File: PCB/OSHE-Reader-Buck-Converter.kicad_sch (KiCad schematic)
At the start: 18 parts, among them U1 TPS5432DDA

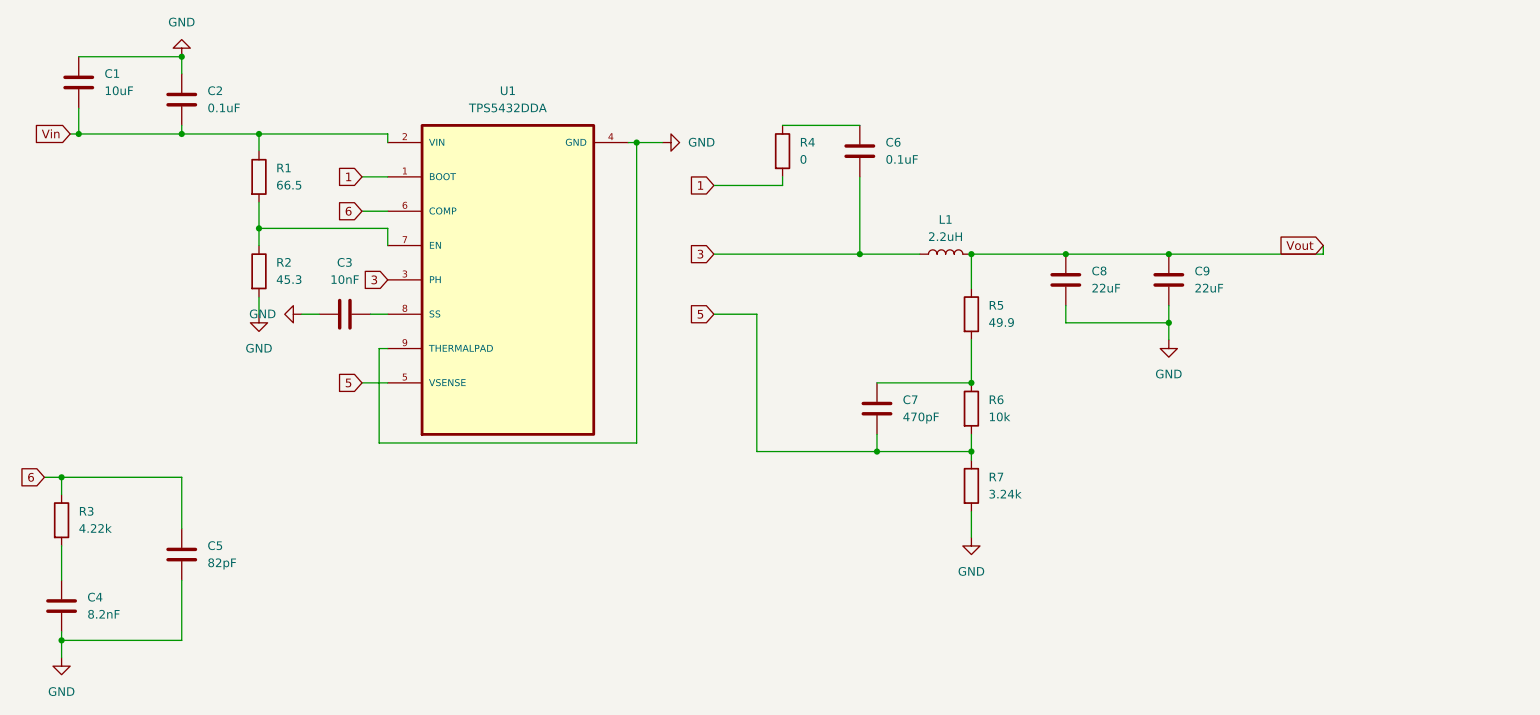
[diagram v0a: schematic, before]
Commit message: added hierarchical symbols to Buck, and did miscelaneous fixes
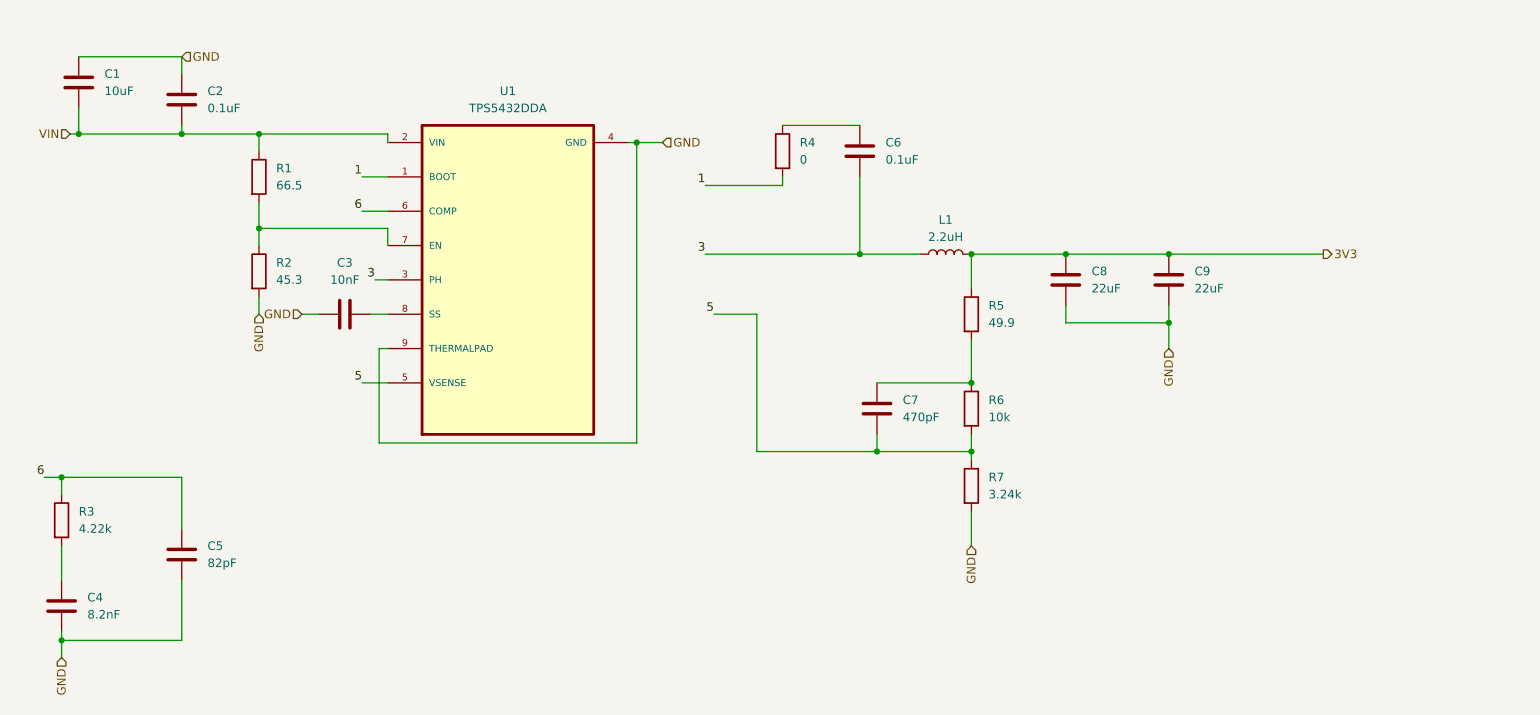
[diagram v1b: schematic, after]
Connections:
- net Vin  renamed VIN
- net Vout renamed 3V3

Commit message: fixed up the pcb so everything is *basically* passing ERC
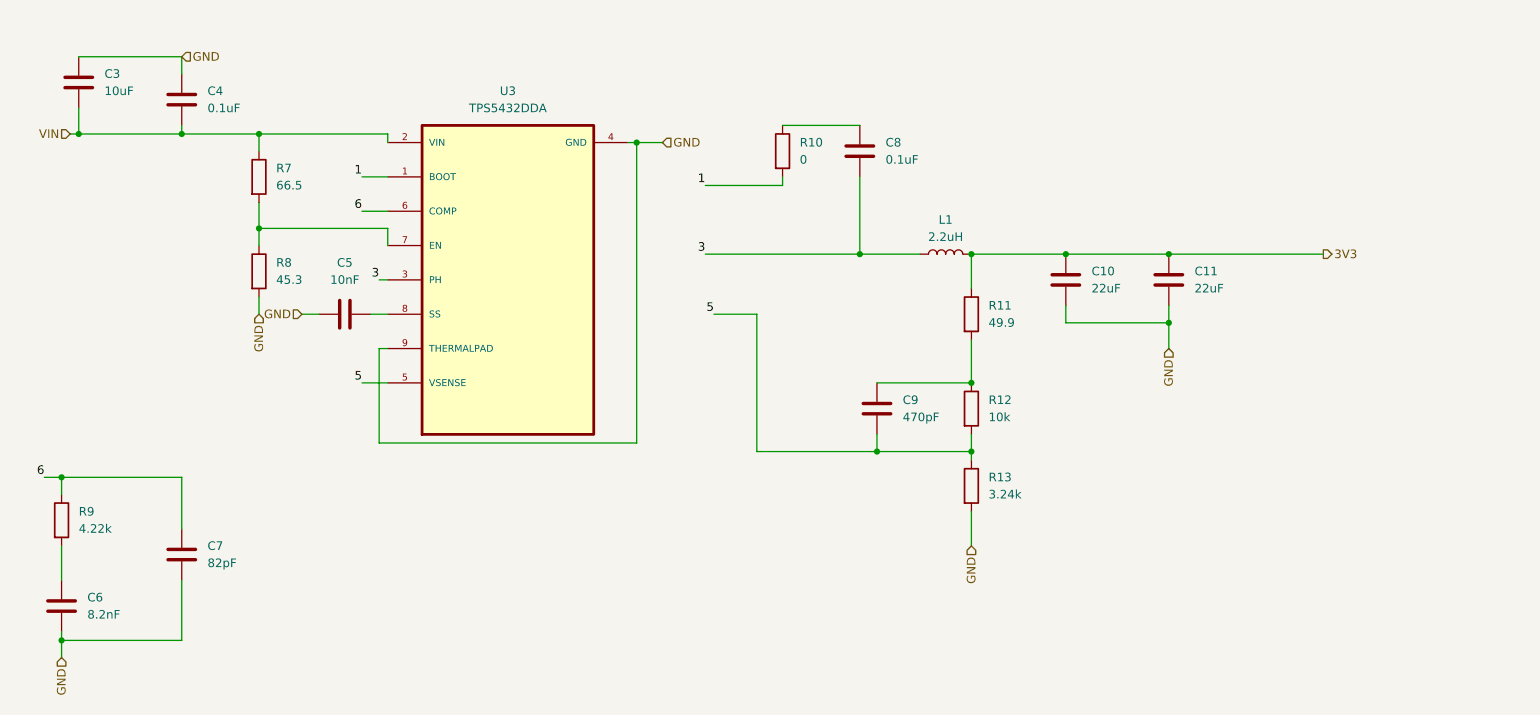
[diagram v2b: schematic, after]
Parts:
- U3: renamed from U1; footprint TPS5432DDA:VREG_LM5017MR_NOPB -> TPS5432DDAR:DDA_R-PDSO-G8_TEX
- renumbered C8 to C10, C9 to C11, C1 to C3, C2 to C4, C3 to C5, C4 to C6, C5 to C7, C6 to C8, C7 to C9, R4 to R10, R5 to R11, R6 to R12, R7 to R13, R1 to R7, R2 to R8, R3 to R9
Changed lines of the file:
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@@
 	(wire
 		(pts
-			(xy 75.565 48.26) (xy 77.47 48.26)
+			(xy 76.2 48.26) (xy 77.47 48.26)
 		)
 		(stroke
@@
 	)
 	(label "3"
-		(at 75.565 48.26 180)
+		(at 76.2 48.26 180)
 		(effects
 			(font
@@
 		(dnp no)
 		(fields_autoplaced yes)
-		(property "Reference" "R3"
+		(property "Reference" "R9"
 			(at 31.75 82.5499 0)
 			(effects
@@
 			(project "OSHE-Reader-PCB"
 				(path "/3f072c92-e35a-4654-839b-728bd3dc3a46/ae251da9-64d7-46e8-9279-c40d7a440224"
-					(reference "R3")
+					(reference "R9")
 					(unit 1)
 				)
@@
 		(dnp no)
 		(fields_autoplaced yes)
-		(property "Reference" "C9"
+		(property "Reference" "C11"
 			(at 196.85 46.9899 0)
 			(effects
@@
 			(project "OSHE-Reader-PCB"
 				(path "/3f072c92-e35a-4654-839b-728bd3dc3a46/ae251da9-64d7-46e8-9279-c40d7a440224"
-					(reference "C9")
+					(reference "C11")
 					(unit 1)
 				)
@@
 		(dnp no)
 		(fields_autoplaced yes)
-		(property "Reference" "C8"
+		(property "Reference" "C10"
 			(at 181.61 46.9899 0)
 			(effects
@@
 			(project "OSHE-Reader-PCB"
 				(path "/3f072c92-e35a-4654-839b-728bd3dc3a46/ae251da9-64d7-46e8-9279-c40d7a440224"
-					(reference "C8")
+					(reference "C10")
 					(unit 1)
 				)
@@
 		(dnp no)
 		(fields_autoplaced yes)
-		(property "Reference" "R4"
+		(property "Reference" "R10"
 			(at 138.43 27.9399 0)
 			(effects
@@
 			(project "OSHE-Reader-PCB"
 				(path "/3f072c92-e35a-4654-839b-728bd3dc3a46/ae251da9-64d7-46e8-9279-c40d7a440224"
-					(reference "R4")
+					(reference "R10")
 					(unit 1)
 				)
@@
 		(dnp no)
 		(fields_autoplaced yes)
-		(property "Reference" "C5"
+		(property "Reference" "C7"
 			(at 50.8 87.6299 0)
 			(effects
@@
 			(project "OSHE-Reader-PCB"
 				(path "/3f072c92-e35a-4654-839b-728bd3dc3a46/ae251da9-64d7-46e8-9279-c40d7a440224"
-					(reference "C5")
+					(reference "C7")
 					(unit 1)
 				)
@@
 		(dnp no)
 		(fields_autoplaced yes)
-		(property "Reference" "R7"
+		(property "Reference" "R13"
 			(at 166.37 77.4699 0)
 			(effects
@@
 			(project "OSHE-Reader-PCB"
 				(path "/3f072c92-e35a-4654-839b-728bd3dc3a46/ae251da9-64d7-46e8-9279-c40d7a440224"
-					(reference "R7")
+					(reference "R13")
 					(unit 1)
 				)
@@
 		(dnp no)
 		(fields_autoplaced yes)
-		(property "Reference" "R1"
+		(property "Reference" "R7"
 			(at 60.96 31.7499 0)
 			(effects
@@
 			(project "OSHE-Reader-PCB"
 				(path "/3f072c92-e35a-4654-839b-728bd3dc3a46/ae251da9-64d7-46e8-9279-c40d7a440224"
-					(reference "R1")
+					(reference "R7")
 					(unit 1)
 				)
@@
 		(dnp no)
 		(fields_autoplaced yes)
-		(property "Reference" "R2"
+		(property "Reference" "R8"
 			(at 60.96 45.7199 0)
 			(effects
@@
 			(project "OSHE-Reader-PCB"
 				(path "/3f072c92-e35a-4654-839b-728bd3dc3a46/ae251da9-64d7-46e8-9279-c40d7a440224"
-					(reference "R2")
+					(reference "R8")
 					(unit 1)
 				)
@@
 		(dnp no)
 		(fields_autoplaced yes)
-		(property "Reference" "C4"
+		(property "Reference" "C6"
 			(at 33.02 95.2499 0)
 			(effects
@@
 			(project "OSHE-Reader-PCB"
 				(path "/3f072c92-e35a-4654-839b-728bd3dc3a46/ae251da9-64d7-46e8-9279-c40d7a440224"
-					(reference "C4")
+					(reference "C6")
 					(unit 1)
 				)
@@
 		(dnp no)
 		(fields_autoplaced yes)
-		(property "Reference" "R6"
+		(property "Reference" "R12"
 			(at 166.37 66.0399 0)
 			(effects
@@
 			(project "OSHE-Reader-PCB"
 				(path "/3f072c92-e35a-4654-839b-728bd3dc3a46/ae251da9-64d7-46e8-9279-c40d7a440224"
-					(reference "R6")
+					(reference "R12")
 					(unit 1)
 				)
@@
 		(dnp no)
 		(fields_autoplaced yes)
-		(property "Reference" "R5"
+		(property "Reference" "R11"
 			(at 166.37 52.0699 0)
 			(effects
@@
 			(project "OSHE-Reader-PCB"
 				(path "/3f072c92-e35a-4654-839b-728bd3dc3a46/ae251da9-64d7-46e8-9279-c40d7a440224"
-					(reference "R5")
+					(reference "R11")
 					(unit 1)
 				)
@@
 		(dnp no)
 		(fields_autoplaced yes)
-		(property "Reference" "C2"
+		(property "Reference" "C4"
 			(at 50.8 20.3199 0)
 			(effects
@@
 			(project "OSHE-Reader-PCB"
 				(path "/3f072c92-e35a-4654-839b-728bd3dc3a46/ae251da9-64d7-46e8-9279-c40d7a440224"
-					(reference "C2")
+					(reference "C4")
 					(unit 1)
 				)
@@
 		(dnp no)
 		(fields_autoplaced yes)
-		(property "Reference" "C3"
+		(property "Reference" "C5"
 			(at 71.12 45.72 90)
 			(effects
@@
 			(project "OSHE-Reader-PCB"
 				(path "/3f072c92-e35a-4654-839b-728bd3dc3a46/ae251da9-64d7-46e8-9279-c40d7a440224"
-					(reference "C3")
+					(reference "C5")
 					(unit 1)
 				)
@@
 		(dnp no)
 		(fields_autoplaced yes)
-		(property "Reference" "C1"
+		(property "Reference" "C3"
 			(at 35.56 17.7799 0)
 			(effects
@@
 			(project "OSHE-Reader-PCB"
 				(path "/3f072c92-e35a-4654-839b-728bd3dc3a46/ae251da9-64d7-46e8-9279-c40d7a440224"
-					(reference "C1")
+					(reference "C3")
 					(unit 1)
 				)
@@
 		(dnp no)
 		(fields_autoplaced yes)
-		(property "Reference" "C6"
+		(property "Reference" "C8"
 			(at 151.13 27.9399 0)
 			(effects
@@
 			(project "OSHE-Reader-PCB"
 				(path "/3f072c92-e35a-4654-839b-728bd3dc3a46/ae251da9-64d7-46e8-9279-c40d7a440224"
-					(reference "C6")
+					(reference "C8")
 					(unit 1)
 				)
@@
 		(dnp no)
 		(fields_autoplaced yes)
-		(property "Reference" "C7"
+		(property "Reference" "C9"
 			(at 153.67 66.0399 0)
 			(effects
@@
 			(project "OSHE-Reader-PCB"
 				(path "/3f072c92-e35a-4654-839b-728bd3dc3a46/ae251da9-64d7-46e8-9279-c40d7a440224"
-					(reference "C7")
+					(reference "C9")
 					(unit 1)
 				)
@@
 		(dnp no)
 		(fields_autoplaced yes)
-		(property "Reference" "U1"
+		(property "Reference" "U3"
 			(at 95.25 20.32 0)
 			(effects
@@
 			)
 		)
-		(property "Footprint" "TPS5432DDA:VREG_LM5017MR_NOPB"
+		(property "Footprint" "TPS5432DDAR:DDA_R-PDSO-G8_TEX"
 			(at 95.25 48.26 0)
 			(effects
@@
 			(project "OSHE-Reader-PCB"
 				(path "/3f072c92-e35a-4654-839b-728bd3dc3a46/ae251da9-64d7-46e8-9279-c40d7a440224"
-					(reference "U1")
-					(unit 1)
-				)
+					(reference "U3")
+					(unit 1)
+				)
